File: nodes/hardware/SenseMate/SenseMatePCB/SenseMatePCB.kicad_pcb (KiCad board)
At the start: 2 copper layers, 28.2 x 57.5 mm, 17 parts, among them J1 Conn_01x04, M1 Motor_DC, Q1 2SC1815, Q2 2SC1815, SW5 SW_DPDT_x2

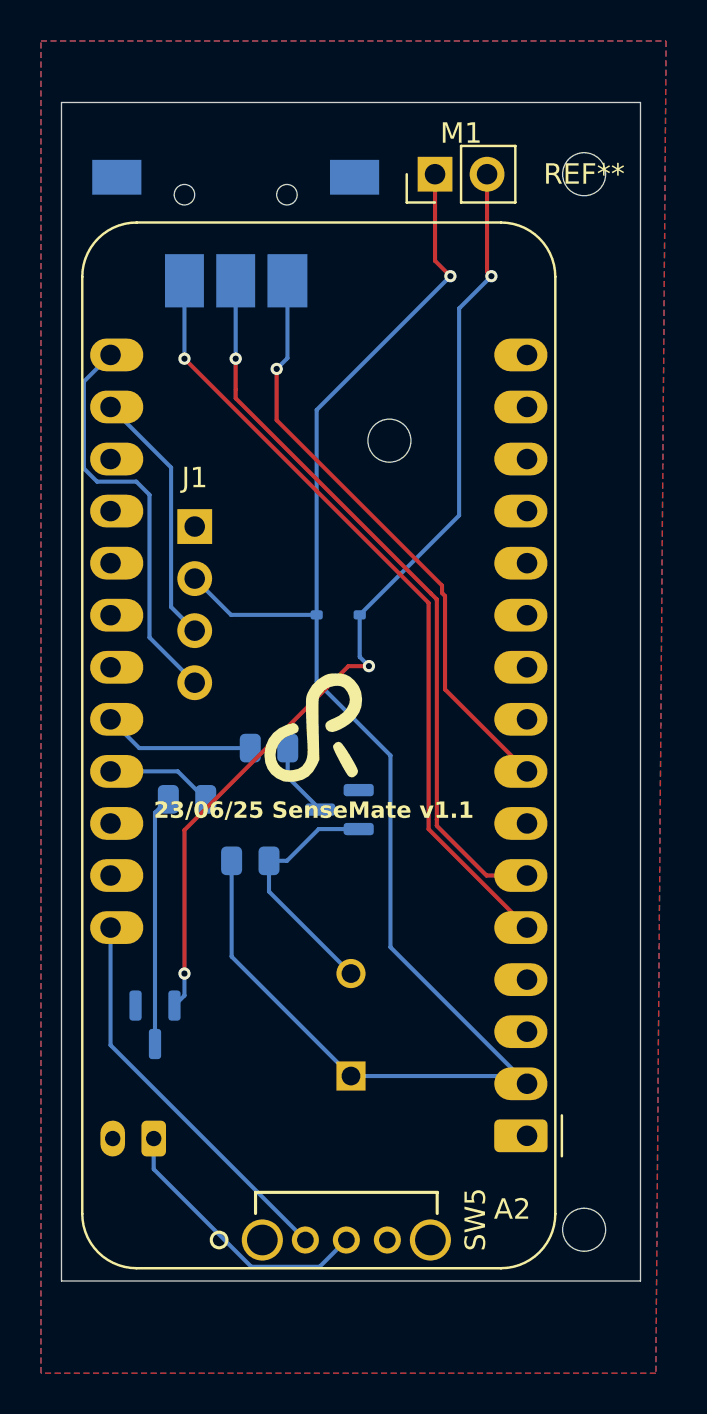
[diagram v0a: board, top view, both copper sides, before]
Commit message: nodes/hardware/sensemate/sensematepcb: ordered version 1.1
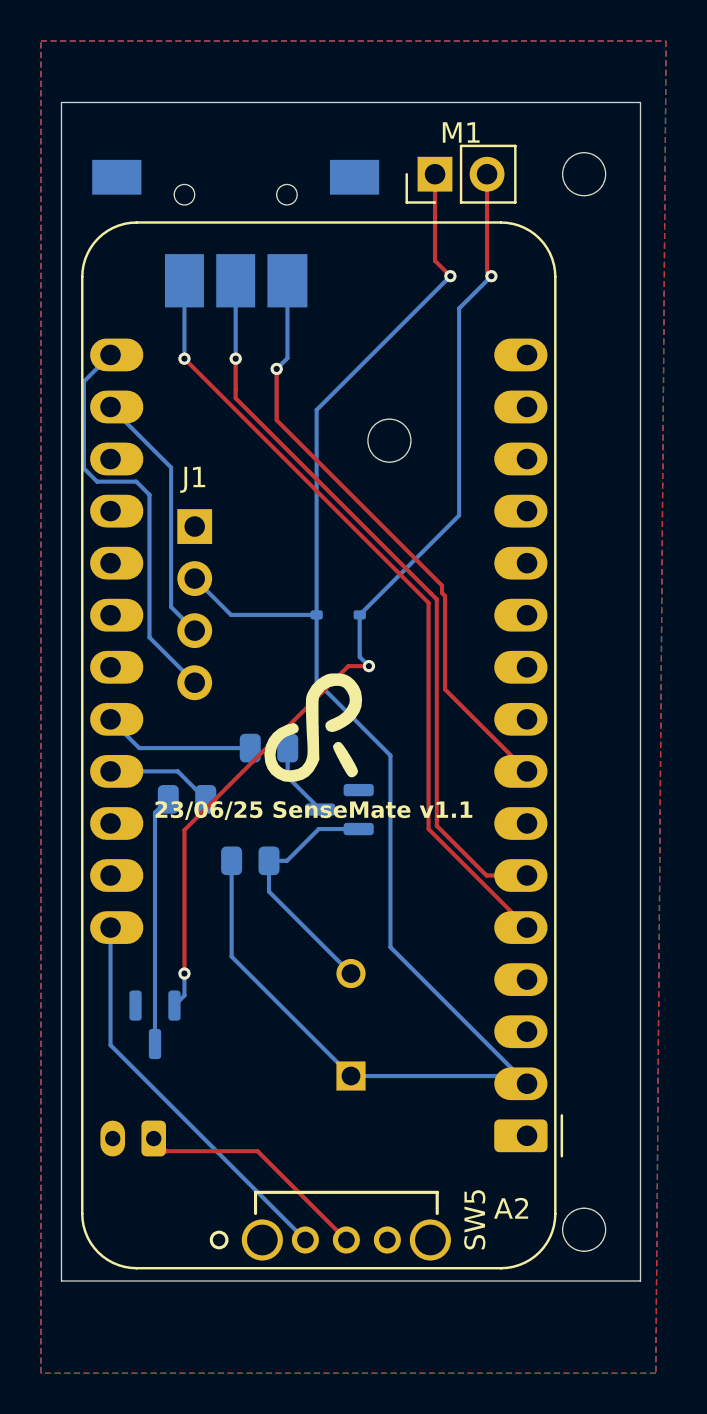
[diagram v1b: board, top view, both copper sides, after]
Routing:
- net Net-(BT1-+): track 13.4 -> 11.5 mm
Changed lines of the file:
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@@
 			(drillshape 0)
 			(scaleselection 1)
-			(outputdirectory "gerber_v1_0/")
+			(outputdirectory "gerber_v1_1/")
 		)
 	)
@@
 			)
 		)
-		(attr through_hole)
+		(attr through_hole allow_missing_courtyard)
 		(fp_line
 			(start -2.4323 -2.3241)
@@
 		)
 		(clearance 0.2)
-		(attr through_hole)
+		(attr through_hole allow_missing_courtyard)
 		(fp_line
 			(start 21.7 -3.81)
@@
 			(layer "F.CrtYd")
 		)
-		(fp_text user "${REFERENCE}"
-			(at 0 0 0)
-			(layer "F.Fab")
-			(effects
-				(font
-					(size 1 1)
-					(thickness 0.15)
-				)
-			)
-		)
 		(pad "" np_thru_hole circle
 			(at 0 0)
@@
 			(at 0 0 0)
 			(layer "F.SilkS")
+			(hide yes)
 			(effects
 				(font
@@
 			(layer "F.CrtYd")
 		)
-		(fp_text user "${REFERENCE}"
-			(at 0 0 0)
-			(layer "F.Fab")
-			(effects
-				(font
-					(size 1 1)
-					(thickness 0.15)
-				)
-			)
-		)
 		(pad "" np_thru_hole circle
 			(at 0 0)
@@
 			(layer "F.CrtYd")
 		)
-		(fp_text user "${REFERENCE}"
-			(at 0 0 0)
-			(layer "F.Fab")
-			(effects
-				(font
-					(size 1 1)
-					(thickness 0.15)
-				)
-			)
-		)
 		(pad "" np_thru_hole circle
 			(at 0 0)
@@
 		(attr through_hole)
 		(fp_line
-			(start 5.9 5.9)
-			(end 5.9 2)
+			(start -2.6 -6.3)
+			(end -2.6 -6.3)
 			(stroke
 				(width 0.2)
@@
 		)
 		(fp_line
-			(start 5.9 -0.2)
-			(end 5.9 -5.9)
+			(start -2.6 -6.4)
+			(end -2.6 -6.4)
 			(stroke
 				(width 0.2)
@@
 		)
 		(fp_line
-			(start 5.9 -5.9)
-			(end -5.9 -5.9)
+			(start -2.6 -6.4)
+			(end -2.6 -6.4)
 			(stroke
 				(width 0.2)
@@
 			(layer "B.SilkS")
 		)
-		(fp_line
+		(fp_arc
 			(start -2.6 -6.3)
-			(end -2.6 -6.3)
+			(mid -2.65 -6.35)
+			(end -2.6 -6.4)
 			(stroke
 				(width 0.2)
@@
 			(layer "B.SilkS")
 		)
-		(fp_line
+		(fp_arc
 			(start -2.6 -6.4)
-			(end -2.6 -6.4)
+			(mid -2.55 -6.35)
+			(end -2.6 -6.3)
 			(stroke
 				(width 0.2)
@@
 			(layer "B.SilkS")
 		)
-		(fp_line
+		(fp_arc
 			(start -2.6 -6.4)
-			(end -2.6 -6.4)
+			(mid -2.55 -6.35)
+			(end -2.6 -6.3)
 			(stroke
 				(width 0.2)
@@
 		)
 		(fp_line
-			(start -5.9 5.9)
-			(end 5.9 5.9)
+			(start 5.9 5.9)
+			(end 5.9 2)
 			(stroke
 				(width 0.2)
 				(type solid)
 			)
-			(layer "B.SilkS")
+			(layer "Dwgs.User")
 		)
 		(fp_line
-			(start -5.9 2)
-			(end -5.9 5.9)
+			(start 5.9 -0.2)
+			(end 5.9 -5.9)
 			(stroke
 				(width 0.2)
 				(type solid)
 			)
-			(layer "B.SilkS")
+			(layer "Dwgs.User")
 		)
 		(fp_line
-			(start -5.9 -5.9)
-			(end -5.9 -0.2)
+			(start 5.9 -5.9)
+			(end -5.9 -5.9)
 			(stroke
 				(width 0.2)
 				(type solid)
 			)
-			(layer "B.SilkS")
+			(layer "Dwgs.User")
 		)
-		(fp_arc
-			(start -2.6 -6.3)
-			(mid -2.65 -6.35)
-			(end -2.6 -6.4)
+		(fp_line
+			(start -5.9 5.9)
+			(end 5.9 5.9)
 			(stroke
 				(width 0.2)
 				(type solid)
 			)
-			(layer "B.SilkS")
+			(layer "Dwgs.User")
 		)
-		(fp_arc
-			(start -2.6 -6.4)
-			(mid -2.55 -6.35)
-			(end -2.6 -6.3)
+		(fp_line
+			(start -5.9 2)
+			(end -5.9 5.9)
 			(stroke
 				(width 0.2)
 				(type solid)
 			)
-			(layer "B.SilkS")
+			(layer "Dwgs.User")
 		)
-		(fp_arc
-			(start -2.6 -6.4)
-			(mid -2.55 -6.35)
-			(end -2.6 -6.3)
+		(fp_line
+			(start -5.9 -5.9)
+			(end -5.9 -0.2)
 			(stroke
 				(width 0.2)
 				(type solid)
 			)
-			(layer "B.SilkS")
+			(layer "Dwgs.User")
 		)
 		(fp_line
@@
 	)
 	(segment
-		(start 97.5 107.044557)
+		(start 98.119999 106.169999)
 		(end 97.5 105.55)
 		(width 0.2)
-		(layer "B.Cu")
-		(net 27)
-	)
-	(segment
-		(start 102.259743 111.8043)
-		(end 97.5 107.044557)
-		(width 0.2)
-		(layer "B.Cu")
+		(layer "F.Cu")
 		(net 27)
 	)
 	(segment
-		(start 106.900001 110.5)
-		(end 105.595701 111.8043)
+		(start 102.57 106.169999)
+		(end 98.119999 106.169999)
 		(width 0.2)
-		(layer "B.Cu")
+		(layer "F.Cu")
 		(net 27)
 	)
 	(segment
-		(start 105.595701 111.8043)
-		(end 102.259743 111.8043)
+		(start 102.57 106.169999)
+		(end 106.900001 110.5)
 		(width 0.2)
-		(layer "B.Cu")
+		(layer "F.Cu")
 		(net 27)
 	)
